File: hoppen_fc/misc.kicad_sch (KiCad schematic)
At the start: 10 parts

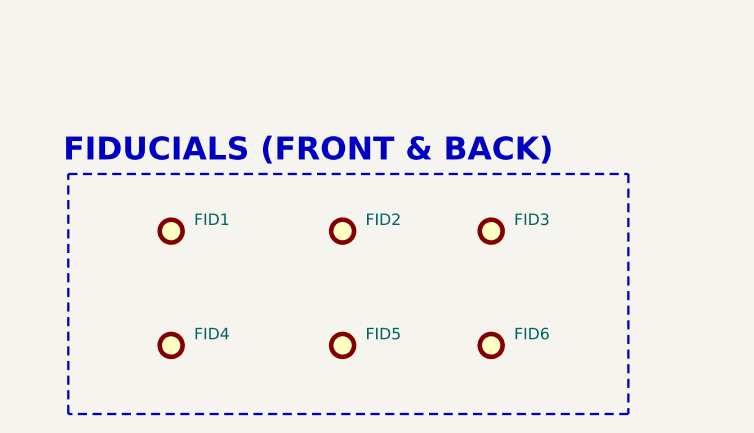
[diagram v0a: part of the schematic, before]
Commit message: finished adding lcsc numbers
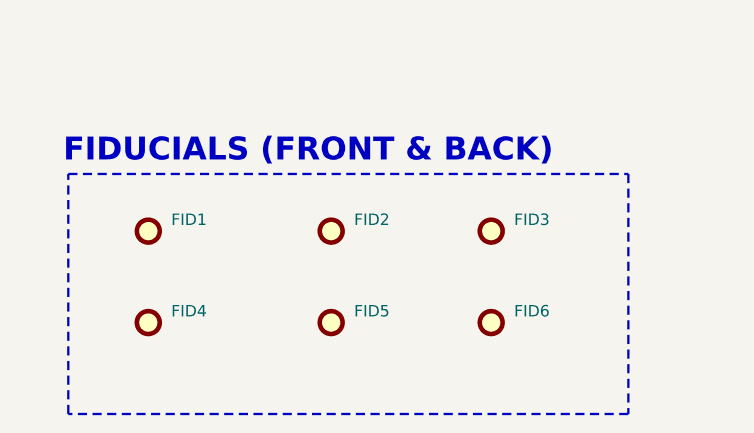
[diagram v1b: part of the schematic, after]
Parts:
- FID1, FID2, FID3, FID4, FID5, FID6: footprint Fiducial:Fiducial_1mm_Mask3mm -> Fiducial:Fiducial_1mm_Mask2mm

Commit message: ready for routing?
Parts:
- H1, H2, H3, H4: footprint MountingHole:MountingHole_3.2mm_M3_Pad_Via -> 0_misc:MountingHole_3.2mm_M3_Pad_Via

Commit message: comments
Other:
- note added: "ADD LOGO AND HOPPEN LOGO"
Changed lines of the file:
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@@
+		)
+	)
+	(text "ADD LOGO AND HOPPEN LOGO"
+		(exclude_from_sim no)
+		(at 216.154 49.53 0)
+		(effects
+			(font
+				(face "KiCad Font")
+				(size 2.54 2.54)
+				(thickness 0.508)
+				(bold yes)
+				(color 255 0 0 1)
+			)
 		)
 	)

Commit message: bump
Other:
- note removed: "ADD LOGO AND HOPPEN LOGO"
- note removed: "Logos and Graphics"
- moved on the sheet: FID1, FID2, FID3, FID4, FID5, FID6, H1, H2, H3, H4
